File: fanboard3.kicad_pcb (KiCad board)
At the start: 2 copper layers, 65 x 56 mm, 28 parts, among them J1 PWR IN, J10 Conn_01x14_Male, J11 USB_A, J12 Conn_01x02_Male, J2 Conn_02x08_Odd_Even, J6 FAN1, J7 FAN2, J8 FAN3, J9 FAN4, K1 G6K-2, M1 5V, M2 12V, P1 Conn_02x20_Odd_Even, Q1 2SD1047, U1 SN74HCT245

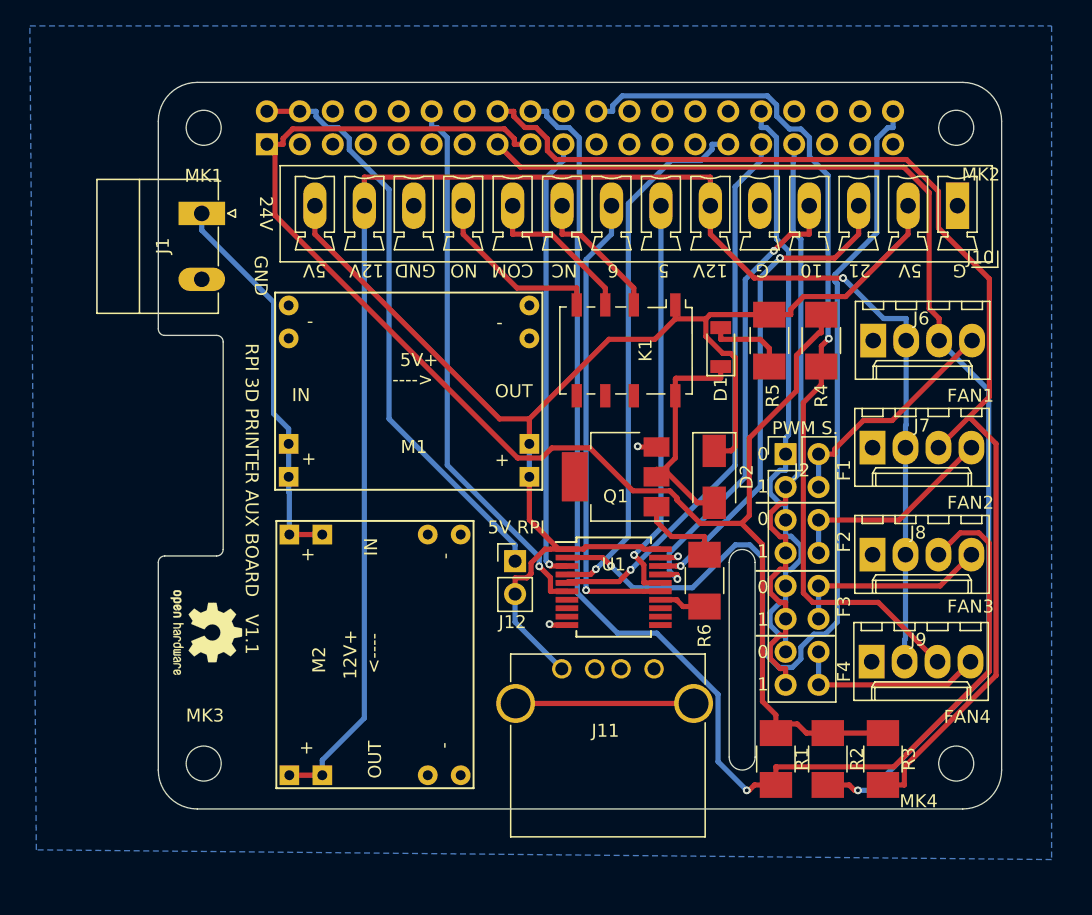
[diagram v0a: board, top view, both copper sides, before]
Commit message: added Volt meter and changed layout
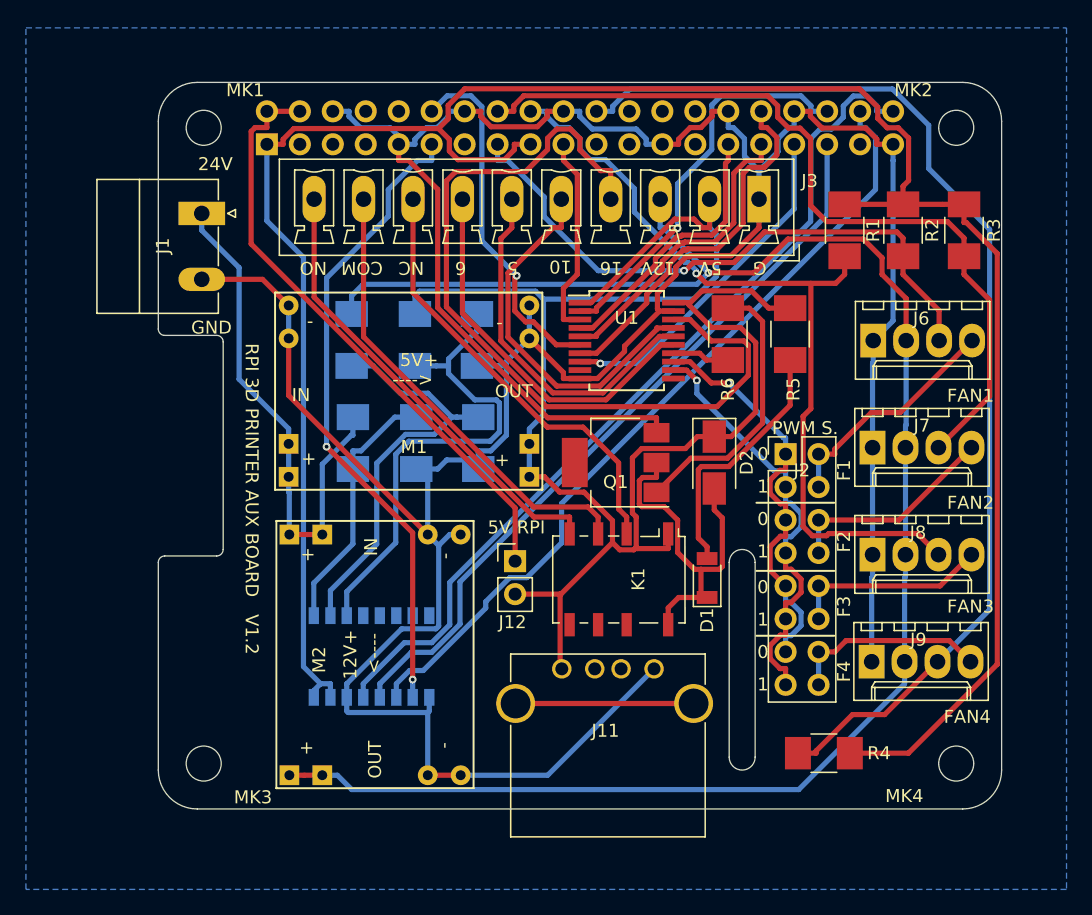
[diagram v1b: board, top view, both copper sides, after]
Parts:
- removed J10: Conn_01x14_Male, Connectors_Phoenix:PhoenixContact_MCV-G_14x3.81mm_Vertical
- removed REF***: OSHW-Logo2_7.3x6mm_SilkScreen, Symbols:OSHW-Logo2_7.3x6mm_SilkScreen
- added J3: Conn_01x10_Male, Connectors_Phoenix:PhoenixContact_MCV-G_10x3.81mm_Vertical, F.Cu at (246.3, 103.0)
- added R10: 10K, Resistors_SMD:R_1210_HandSoldering, B.Cu at (224.7, 121.8)
- added R11: 100K, Resistors_SMD:R_1210_HandSoldering, B.Cu at (219.8, 113.8)
- added R12: 10K, Resistors_SMD:R_1210_HandSoldering, B.Cu at (224.6, 113.8)
- added R7: 100K, Resistors_SMD:R_1210_HandSoldering, B.Cu at (215.0, 121.8)
- added R8: 10K, Resistors_SMD:R_1210_HandSoldering, B.Cu at (219.9, 121.8)
- added R9: 100K, Resistors_SMD:R_1210_HandSoldering, B.Cu at (214.9, 113.8)
- added U2: MCP3008, Housings_SSOP:SOP-16_4.4x10.4mm_Pitch1.27mm, B.Cu at (216.4, 138.2)
- moved R3 41.2 mm to (262.1, 105.4)
- moved R2 41.2 mm to (257.4, 105.4)
- moved R1 41.1 mm to (252.9, 105.4)
- moved R4 31.8 mm to (251.3, 145.7), turned to 180 degrees
- moved R6 19.1 mm to (243.9, 113.4)
- moved U1 19.0 mm to (236.1, 113.9)
- moved D1 17.8 mm to (242.3, 132.2)
- moved K1 17.7 mm to (235.5, 132.3)
- moved R5 1.68 mm to (248.7, 113.4)
- moved D2 1.10 mm to (242.8, 123.3)
- moved Q1 1.10 mm to (235.2, 123.3)
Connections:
- net /GPIO10(SPI0_MOSI) renamed GPI010
- net /GPIO18(GEN1)(PWM0) renamed GPIO18
- net /GPIO22(GEN3) renamed FAN1-RPM
- net /GPIO23(GEN4) renamed FAN2-RPM
- net /GPIO24(GEN5) renamed FAN3-RPM
- net /GPIO5 renamed GPIO5
- net /GPIO6 renamed GPIO6
- net 12V renamed +12V
- net 5V renamed +5V
- net Net-(J2-Pad10) renamed FAN3-PWM
- net Net-(J2-Pad14) renamed FAN4-PWM
- net Net-(J2-Pad2) renamed FAN1-PWM
- net Net-(J2-Pad6) renamed FAN2-PWM
- net Net-(P1-Pad13) renamed /GPIO27(GEN2)
- net Net-(P1-Pad37) renamed /GPIO26
- J2 pad 1: /GPIO12(PWM0) -> PWM0-5V
- J2 pad 11: /GPIO13(PWM1) -> PWM1-5V
- J2 pad 13: /GPIO12(PWM0) -> PWM0-5V
- J2 pad 15: /GPIO13(PWM1) -> PWM1-5V
- J2 pad 3: /GPIO13(PWM1) -> PWM1-5V
- J2 pad 5: /GPIO12(PWM0) -> PWM0-5V
- J2 pad 7: /GPIO13(PWM1) -> PWM1-5V
- J2 pad 9: /GPIO12(PWM0) -> PWM0-5V
- J9 pad 3: /GPIO25(GEN6) -> FAN4-RPM
- P1 pad 11: /GPIO17(GEN0) -> GPIO17
- P1 pad 22: /GPIO25(GEN6) -> FAN4-RPM
- P1 pad 32: /GPIO12(PWM0) -> PWM0
- P1 pad 33: /GPIO13(PWM1) -> PWM1
- P1 pad 35: /GPIO19(SPI1_MISO) -> MISO
- P1 pad 36: /GPIO16 -> GPIO16
- P1 pad 38: /GPIO20(SPI1_MOSI) -> MOSI
- P1 pad 40: /GPIO21(SPI1_SCK) -> SCLK
- R4 pad 1: /GPIO25(GEN6) -> +3V3
- R4 pad 2: +3V3 -> FAN4-RPM
- U1 pad 12: Net-(U1-Pad12) -> PWM1-5V
- U1 pad 13: Net-(U1-Pad13) -> PWM0-5V
- U1 pad 15: Net-(J10-Pad8) -> B4
- U1 pad 16: Net-(J10-Pad7) -> B3
- U1 pad 17: Net-(J10-Pad4) -> B2
- U1 pad 18: Net-(J10-Pad3) -> B1
- U1 pad 2: /GPIO21(SPI1_SCK) -> GPIO16
- U1 pad 7: Net-(U1-Pad7) -> PWM0
- U1 pad 8: Net-(U1-Pad8) -> PWM1
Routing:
- net GND: track 4.26 -> 277.3 mm, vias 3 -> 0
- net FAN4-RPM: track 0.00 -> 86.4 mm
- net /GPIO21(SPI1_SCK): track 74.8 -> 0.00 mm, vias 1 -> 0
- net /GPIO25(GEN6): track 68.1 -> 0.00 mm, vias 1 -> 0
- net SCLK: track 0.00 -> 67.5 mm
- net B1: track 0.00 -> 65.0 mm
- net MOSI: track 0.00 -> 62.6 mm
- net MISO: track 0.00 -> 57.8 mm
- net +3V3: track 118.4 -> 175.2 mm
- net GPIO17: track 0.00 -> 49.4 mm, vias 0 -> 2
- net /GPIO12(PWM0): track 47.3 -> 0.00 mm
- net /GPIO13(PWM1): track 46.8 -> 0.00 mm
- net FAN1-RPM: track 90.0 -> 47.4 mm
- net Net-(R11-Pad2): track 0.00 -> 38.0 mm
- net Net-(J10-Pad3): track 37.5 -> 0.00 mm, vias 2 -> 0
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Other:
- board text added: "16"
- board text added: "RPI 3D PRINTER AUX BOARD V1.2"
- board text removed: "21"
- board text removed: "RPI 3D PRINTER AUX BOARD V1.1"
